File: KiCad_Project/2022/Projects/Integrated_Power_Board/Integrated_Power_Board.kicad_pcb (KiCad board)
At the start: 2 copper layers, 56 x 53.3 mm, 0 parts

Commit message: 部品の配置
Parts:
- added BT1: Battery, Connector_JST:JST_VH_B2P-VH-B_1x02_P3.96mm_Vertical, F.Cu at (125.1, 95.9)
- added C1: CP, Capacitor_THT:C_Radial_D16.0mm_H25.0mm_P7.50mm, F.Cu at (77.7, 66.0)
- added C2: CP, Capacitor_THT:C_Radial_D16.0mm_H25.0mm_P7.50mm, F.Cu at (75.9, 83.6)
- added C3: C, Capacitor_THT:C_Disc_D3.0mm_W1.6mm_P2.50mm, F.Cu at (78.6, 102.0)
- added C4: C, Capacitor_THT:C_Disc_D3.0mm_W1.6mm_P2.50mm, F.Cu at (73.7, 102.2)
- added C5: C, Capacitor_THT:C_Disc_D3.0mm_W1.6mm_P2.50mm, F.Cu at (82.5, 142.9)
- added D1: D_Shockley, Diode_THT:D_DO-201AD_P12.70mm_Horizontal, F.Cu at (137.8, 90.8)
- added D2: LED, LED_THT:LED_D3.0mm_Clear, F.Cu at (100.3, 137.8)
- added D3: D, Diode_THT:D_DO-41_SOD81_P7.62mm_Horizontal, F.Cu at (151.8, 141.0)
- added F1: Fuse, Library:fuse_socket, F.Cu at (121.3, 109.9)
- added FL1: BNX025, Library:FIL_BNX016-01, F.Cu at (188.0, 73.0)
- added J1: Conn_01x02, Connector_JST:JST_XH_B2B-XH-A_1x02_P2.50mm_Vertical, F.Cu at (75.6, 132.7)
- added J2: Conn_01x02, Connector_JST:JST_XH_B2B-XH-A_1x02_P2.50mm_Vertical, F.Cu at (132.1, 113.0)
- added J3: Conn_01x02, Connector_JST:JST_XH_B2B-XH-A_1x02_P2.50mm_Vertical, F.Cu at (132.1, 106.0)
- added J4: Conn_01x02, Connector_JST:JST_XH_B2B-XH-A_1x02_P2.50mm_Vertical, F.Cu at (132.1, 99.1)
- added J5: Conn_01x02, Connector_JST:JST_XH_B2B-XH-A_1x02_P2.50mm_Vertical, F.Cu at (130.8, 52.7)
- added J6: Conn_01x02, Connector_JST:JST_XH_B2B-XH-A_1x02_P2.50mm_Vertical, F.Cu at (130.8, 45.1)
- added MES1: Voltmeter_DC, Library:voltage_counter, F.Cu at (149.2, 111.1)
- added R1: R, Resistor_THT:R_Axial_DIN0207_L6.3mm_D2.5mm_P7.62mm_Horizontal, F.Cu at (90.2, 137.8)
- added R2: R, Resistor_THT:R_Axial_DIN0207_L6.3mm_D2.5mm_P7.62mm_Horizontal, F.Cu at (68.6, 147.3)
- added R3: R, Resistor_THT:R_Axial_DIN0207_L6.3mm_D2.5mm_P7.62mm_Horizontal, F.Cu at (68.6, 137.8)
- added R4: R, Resistor_THT:R_Axial_DIN0207_L6.3mm_D2.5mm_P7.62mm_Horizontal, F.Cu at (98.7, 80.9)
- added R5: R, Resistor_THT:R_Axial_DIN0207_L6.3mm_D2.5mm_P7.62mm_Horizontal, F.Cu at (106.0, 92.1)
- added R6: R, Resistor_THT:R_Axial_DIN0207_L6.3mm_D2.5mm_P7.62mm_Horizontal, F.Cu at (90.0, 92.1)
- added RV1: Varistor, Varistor:RV_Disc_D9mm_W3.3mm_P5mm, F.Cu at (175.3, 95.2)
- added RV2: R_POT_TRIM_US, Potentiometer_THT:Potentiometer_Bourns_3296W_Vertical, F.Cu at (113.6, 74.2)
- added SW1: SW_SPST, Library:DS-850k, F.Cu at (169.5, 108.0)
- added SW2: SW_SPST, Library:toggleswitch, F.Cu at (93.0, 87.0)
- added U1: ATtiny85-20PU, Package_DIP:DIP-8_W7.62mm, F.Cu at (87.6, 140.3)
- added U2: OKL-T_6-W12N-C, Library:DCDC-murata-6A, F.Cu at (102.2, 40.6)
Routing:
- net GND: track 0.00 -> 88.0 mm
- net +12V: track 0.00 -> 35.0 mm
- net Voltage: track 0.00 -> 31.6 mm
- net Net-(BT1-Pad2): track 0.00 -> 13.2 mm

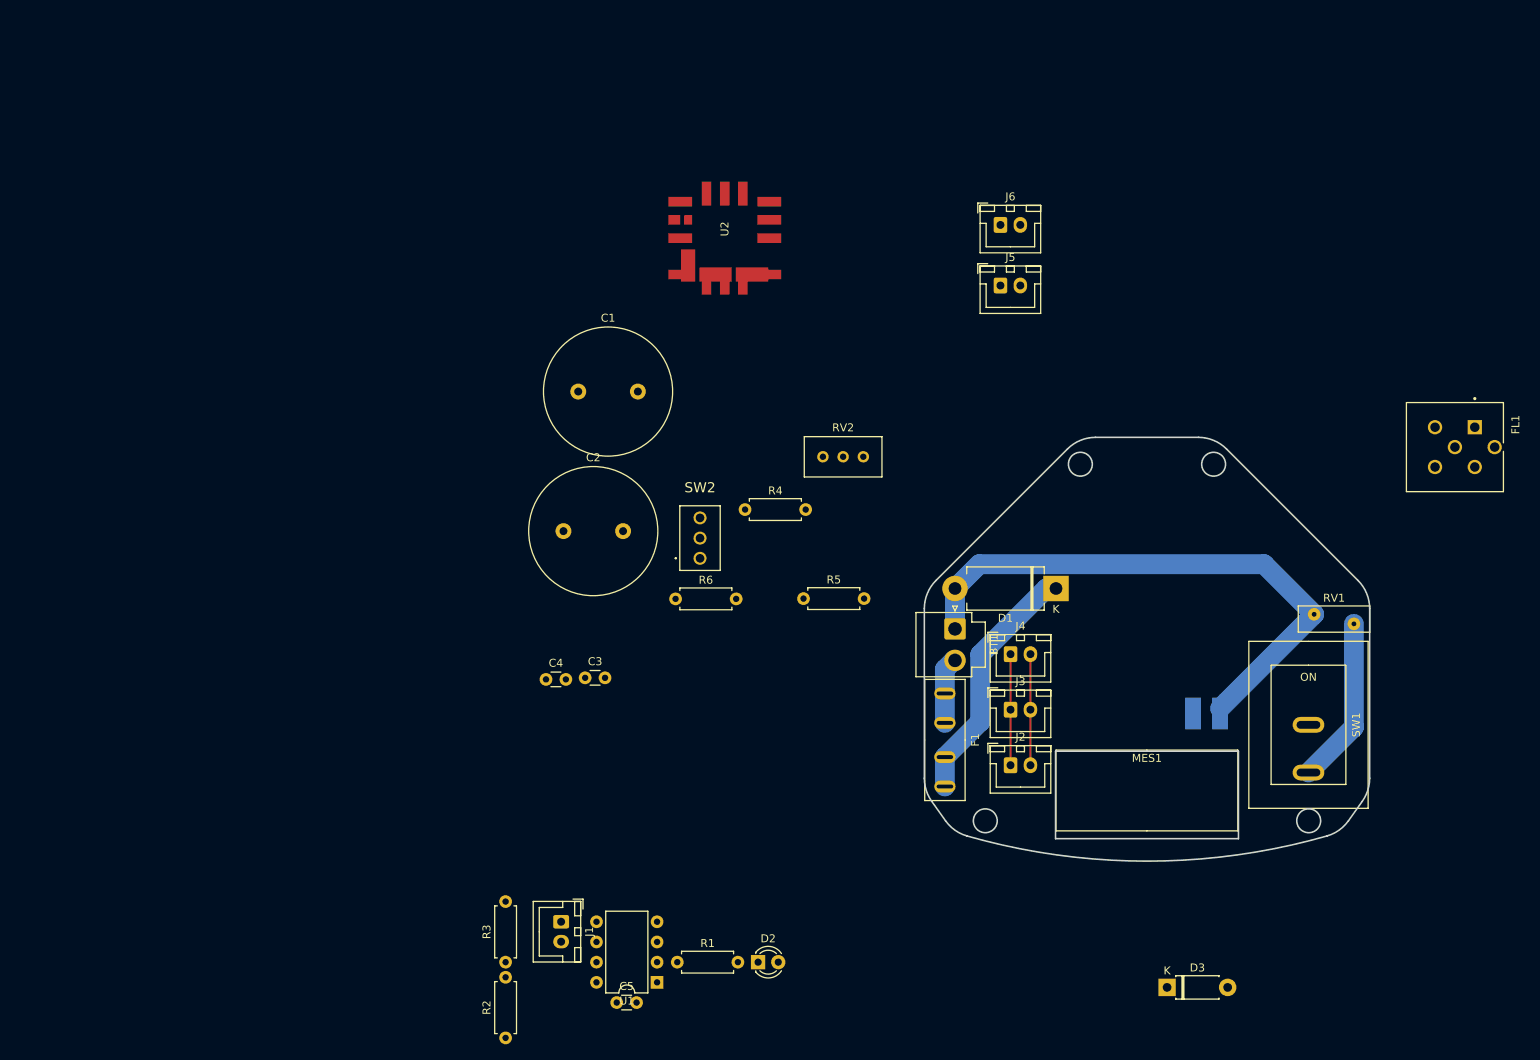
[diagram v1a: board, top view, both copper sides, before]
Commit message: ビアを追加してノイズ対策
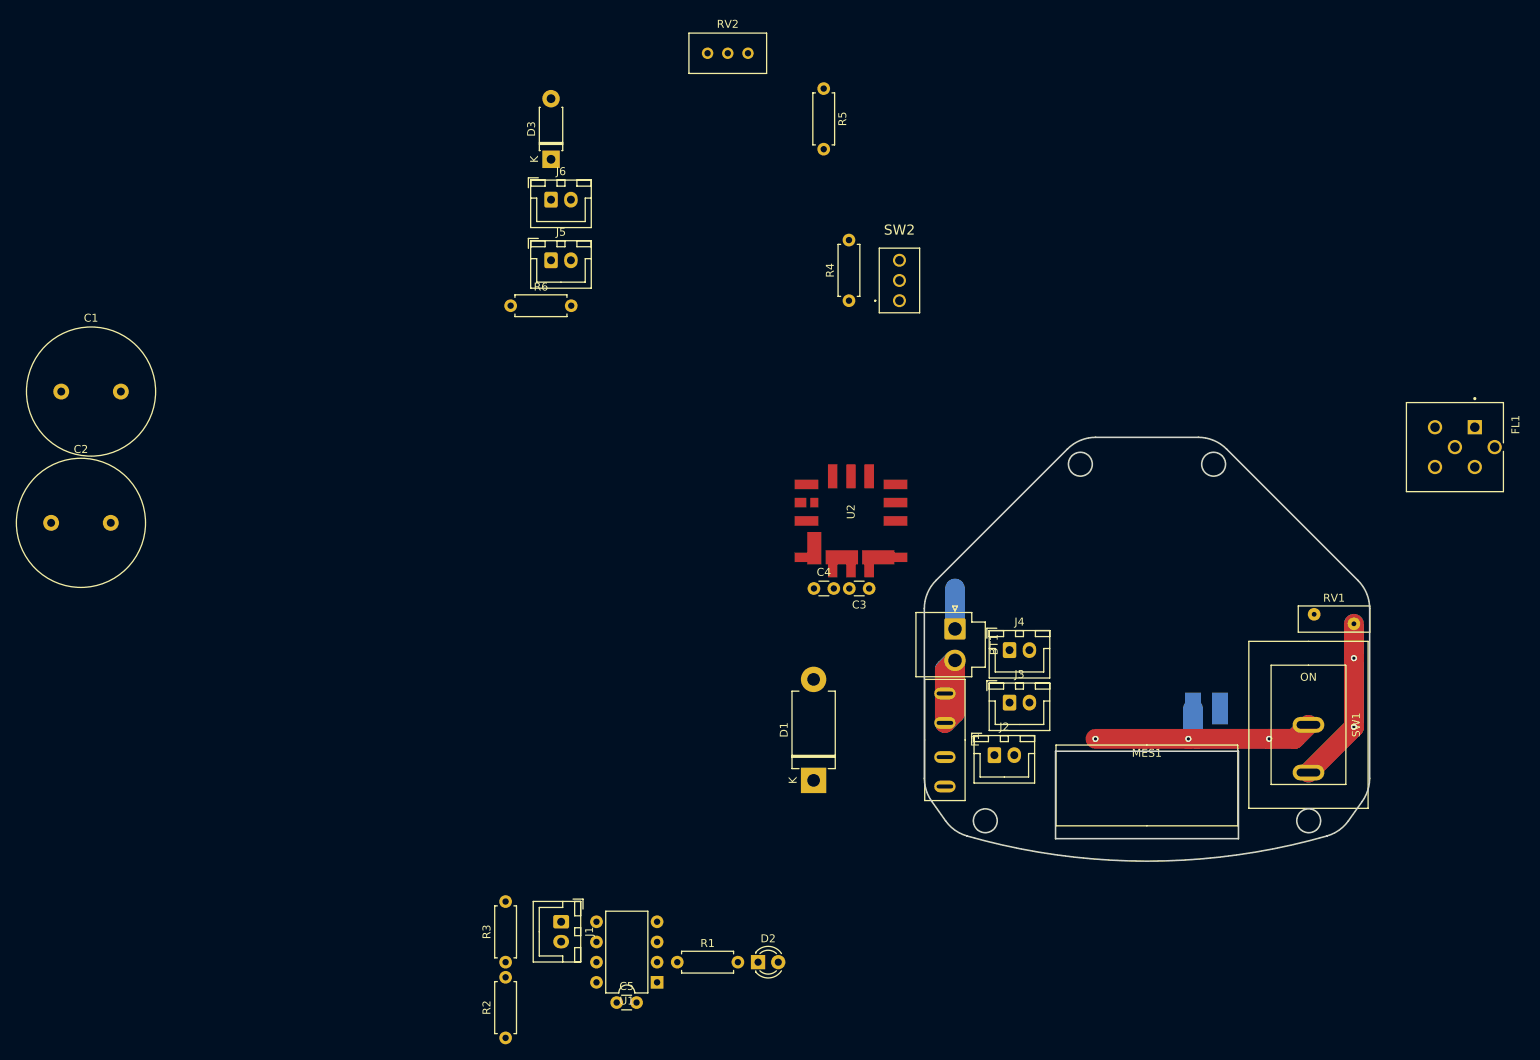
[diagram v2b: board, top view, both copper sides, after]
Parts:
- moved D3 129.8 mm to (74.3, 36.8), turned to 90 degrees
- moved C1 65.0 mm to (12.7, 66.0)
- moved C2 64.4 mm to (11.4, 82.5)
- moved R5 64.2 mm to (108.6, 27.9), turned to 270 degrees
- moved J5 56.6 mm to (74.3, 49.5)
- moved J6 56.6 mm to (74.3, 41.9)
- moved RV2 52.8 mm to (99.1, 23.5)
- moved R6 42.3 mm to (69.2, 55.2)
- moved SW2 41.0 mm to (118.1, 54.6)
- moved U2 38.9 mm to (118.1, 76.2)
- moved D1 38.9 mm to (107.3, 114.9), turned to 90 degrees
- moved C3 37.4 mm to (114.3, 90.8), turned to 180 degrees
- moved C4 35.6 mm to (107.4, 90.8)
- moved R4 29.3 mm to (111.8, 54.6), turned to 90 degrees
- moved J2 2.40 mm to (130.0, 111.8)
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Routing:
- net GND: track 88.0 -> 5.08 mm
- net Net-(BT1-Pad2): track 13.2 -> 38.3 mm
- net Voltage: track 31.6 -> 46.4 mm, vias 0 -> 3
- net +12V: track 35.0 -> 42.1 mm, vias 0 -> 2

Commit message: 統合電源基板の設計の完了
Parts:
- removed C1, C2: CP, Capacitor_THT:C_Radial_D16.0mm_H25.0mm_P7.50mm
- removed D2: LED, LED_THT:LED_D3.0mm_Clear
- removed J4: Conn_01x02, Connector_JST:JST_XH_B2B-XH-A_1x02_P2.50mm_Vertical
- removed R1: R, Resistor_THT:R_Axial_DIN0207_L6.3mm_D2.5mm_P7.62mm_Horizontal
- added ?: , , F.Cu at (178.4, 91.1)
- added ?: , , F.Cu at (153.0, 102.7)
- C3, C4: footprint Capacitor_THT:C_Disc_D3.0mm_W1.6mm_P2.50mm -> Capacitor_THT:C_Disc_D4.3mm_W1.9mm_P5.00mm
- C5: moved to B.Cu
- J1: footprint Connector_JST:JST_XH_B2B-XH-A_1x02_P2.50mm_Vertical -> Connector_PinHeader_2.54mm:PinHeader_1x02_P2.54mm_Vertical
- moved R2 86.9 mm to (145.7, 107.3), turned to 180 degrees
- moved RV2 84.3 mm to (158.9, 82.9), turned to 90 degrees
- moved R5 81.7 mm to (159.9, 91.6)
- moved D3 78.5 mm to (132.7, 89.3)
- moved R3 77.0 mm to (138.0, 104.5), turned to 0 degrees
- moved J6 73.4 mm to (136.8, 80.5)
- moved J5 73.0 mm to (136.8, 87.2)
- moved C5 69.4 mm to (135.0, 97.4)
- moved J1 67.3 mm to (126.4, 88.5), turned to 315 degrees
- moved R6 67.1 mm to (129.7, 84.5), turned to 270 degrees
- moved U1 65.4 mm to (140.1, 101.2)
- moved R4 63.5 mm to (148.0, 106.8), turned to 0 degrees
- moved SW2 56.9 mm to (134.5, 109.1)
- moved C4 48.6 mm to (155.7, 85.9), turned to 180 degrees
- moved J2 40.9 mm to (167.1, 94.5), turned to 180 degrees
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- renumbered U2 to DCDC
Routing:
- net GND: track 5.08 -> 159.5 mm, vias 0 -> 2
- net GND1: track 0.00 -> 138.8 mm, vias 0 -> 2
- net Net-(C2-Pad1): track 0.00 -> 99.8 mm
- net +12V: track 42.1 -> 139.7 mm, vias 2 -> 4
- net Voltage: track 46.4 -> 124.3 mm, vias 3 -> 4
- net Net-(C4-Pad1): track 0.00 -> 47.7 mm
- net +5V: track 0.00 -> 27.6 mm
- net Net-(R4-Pad2): track 0.00 -> 20.5 mm
- net Net-(RV2-Pad3): track 0.00 -> 13.9 mm
- net Net-(R2-Pad2): track 0.00 -> 11.0 mm
- net /RX: track 0.00 -> 10.3 mm
- net Net-(R5-Pad1): track 0.00 -> 9.72 mm
- net /TX: track 0.00 -> 9.32 mm

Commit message: 設計図資料の更新と発注用ファイルの作成
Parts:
- removed ? (x2): , 
- moved R4 7.71 mm to (155.3, 104.5), turned to 180 degrees
- renumbered DCDC to U2
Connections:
- C3 pad 1: Net-(C2-Pad1) -> Net-(C3-Pad1)
- D1 pad 1: Voltage -> Net-(D1-Pad1)
- F1 pad 1: Voltage -> Net-(D1-Pad1)
- FL1 pad 1: +12V -> Voltage
- FL1 pad 2: Net-(C2-Pad1) -> Net-(C3-Pad1)
- J2 pad 1: +12V -> Voltage
- J3 pad 1: +12V -> Voltage
- MES1 pad 2: Voltage -> Net-(D1-Pad1)
- R4 pad 1: Net-(C2-Pad1) -> Net-(R4-Pad1)
- R4 pad 2: Net-(R4-Pad2) -> Net-(C3-Pad1)
- RV1 pad 1: +12V -> Voltage
- SW1 pad 1: Voltage -> Net-(D1-Pad1)
- SW1 pad 2: +12V -> Voltage
- SW2 pad 1: Net-(C2-Pad1) -> Net-(R4-Pad1)
- U2 pad 1: Net-(R4-Pad2) -> Net-(R4-Pad1)
- U2 pad 2: Net-(C2-Pad1) -> Net-(C3-Pad1)
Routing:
- net +12V: track 139.7 -> 0.00 mm, vias 4 -> 0
- net Net-(D1-Pad1): track 0.00 -> 119.5 mm, vias 0 -> 4
- net Net-(C2-Pad1): track 99.8 -> 0.00 mm
- net Net-(C3-Pad1): track 0.00 -> 62.7 mm, vias 0 -> 2
- net Voltage: track 124.3 -> 170.7 mm
- net Net-(R4-Pad1): track 0.00 -> 40.8 mm
- net GND: track 159.5 -> 197.3 mm
- net Net-(R4-Pad2): track 20.5 -> 0.00 mm
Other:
- outline, holes or cut-outs redrawn
- board text added: "MUNAKO Hercules Integrated_Power_Board ver.2022 Designed by kiyo"
